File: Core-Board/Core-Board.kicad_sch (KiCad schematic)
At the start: 21 parts, among them J1 POWER, J2 PCIE, J3 XT60-M, J4 PCIE, J5 PCIE, J6 PCIE, J7 Conn_01x19_Male, J8 PCIE, J9 Conn_01x19_Male, SW1 SW_SPST, U1 AP2112K-3.3, U2 74HC4050D, U3 XTSD04GLGEAG, U4 ESP32-DEVKITC-32D

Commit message: more smol updates
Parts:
- removed C4, C5: 10uF, symbol Device:C_Small
- removed R1: 10k, symbol Device:R_Small
- removed U1: AP2112K-3.3, Package_TO_SOT_SMD:SOT-23-5, symbol Regulator_Linear:AP2112K-3.3
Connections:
- net SD VIN is gone; now on net +3.3V: U2.1 (VCC)
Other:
- moved on the sheet: C1, C2, C3, J1, J3

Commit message: core board pinouts
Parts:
- removed C1, C2, C3: 0.1uF, symbol Device:C_Small
- removed J6: PCIE, symbol PCIE:PCIE-LP-01-01-F-DV-A-TR_(card_edge)
- added C10, C4, C9: 22uF, symbol Device:C_Small
- added C5, C6: 2.2uF, symbol Device:C_Small
- added C7, C8: 0.1uF, symbol Device:C_Small
- added D1, D2, D3, D4, D5: D_Small, symbol Device:D_Small
- added F1, F4: 6A Fuse, symbol Device:Polyfuse_Small
- added F2, F3: 500mA Fuse, symbol Device:Polyfuse_Small
- added J10: PCIE, symbol PCIE:PCIE-LP-01-01-F-DV-A-TR_(card_edge)
- added L1: 12uH, symbol Device:L_Small
- added L2: 18, symbol Device:L_Small
- added R1: 10k, symbol Device:R_Small
- added R3: 51k, symbol Device:R_Small
- added R4, R6: 22.1k, symbol Device:R_Small
- added R5: 88.7k, symbol Device:R_Small
- added R7, R8: 1k, symbol Device:R_Small
- added U1, U4: TPS560430X3FDBVT, Package_TO_SOT_SMD:SOT-23-6, symbol Regulator_Switching:TPS560430X3FDBVT
- R2: value R_Small -> 1k
- renumbered U4 to J6
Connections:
- net +12V: now also F1.1; no longer J2.A16, J2.A17, J2.A18, J2.B16, J2.B17, J2.B18, J4.A16, J4.A17, J4.A18, J4.B16, J4.B17, J4.B18, J5.A16, J5.A17, J5.A18, J5.B16, J5.B17, J5.B18, J8.A16, J8.A17, J8.A18, J8.B16, J8.B17, J8.B18
- net +3.3V: no longer J2.B13, J2.B14, J4.B13, J4.B14, J5.B13, J5.B14, J6.1 (3V3), J8.B13, J8.B14
- net +5V: no longer J2.A13, J2.A14, J4.A13, J4.A14, J5.A13, J5.A14, J6.19 (EXT_5V), J8.A13, J8.A14
- net GND: now also J2.A6, J4.A6, J5.A6, J8.A6, C10.1, C4.1, C5.1, C6.1, C9.1, D1.2 (A), D4.2 (A), D5.2 (A), J10.A12, J10.A15, J10.A3, J10.A6, J10.B12, J10.B15, J10.B3, R4.2, R6.2, U1.2 (GND), U4.2 (GND); no longer J2.A7, J2.B4, J2.B8, J4.A7, J4.B4, J4.B8, J5.A7, J5.B4, J5.B8, J8.A7, J8.B4, J8.B8
- net HX CLK: now also J10.A10
- net HX1: now also J2.B4, J4.B4, J5.B4, J8.B4, J10.B4; no longer J2.A4, J4.A4, J5.A4, J8.A4
- net HX2: now also J2.B5, J4.B5, J5.B5, J8.B5, J10.B5; no longer J2.A5, J4.A5, J5.A5, J8.A5
- net HX3: now also J2.B6, J4.B6, J5.B6, J8.B6, J10.B6; no longer J2.A6, J4.A6, J5.A6, J8.A6
- net HX4: now also J2.B7, J4.B7, J5.B7, J8.B7, J10.B7; no longer J2.B5, J4.B5, J5.B5, J8.B5
- net HX5: now also J2.B8, J4.B8, J5.B8, J8.B8, J10.B8; no longer J2.B6, J4.B6, J5.B6, J8.B6
- net HX6: now also J2.A7, J4.A7, J5.A7, J8.A7, J10.A7; no longer J2.B7, J4.B7, J5.B7, J8.B7
- net HX7: now also J10.A8
- net HX8: now also J10.A9
- net MOS SCL: now also J10.A2
- net MOS SDA: now also J10.A1
- net SD CLK: no longer J6.28 (IO18), J9.9 (Pin_9)
- net SD MISO: no longer J6.21 (IO23), J9.2 (Pin_2)
- net TC CLK: now also J2.A4, J4.A4, J5.A4, J8.A4, J10.A4; no longer J2.B1, J4.B1, J5.B1, J8.B1
- net TC MOSI: no longer J2.B2, J4.B2, J5.B2, J6.15 (IO13), J8.B2
- net TC1: now also J10.B9
- net TC2: now also J10.B10
- net TC3: now also J10.B11
- net TC4: now also J10.A11
- new net: C7.2, U1.1 (CB)
- new net: C7.1, D3.1 (K), L2.1, U1.6 (SW)
- new net: C4.2, F1.2, F4.1, R1.1
- new net: C9.2, D2.2 (A), F2.1, L1.2, R3.1
- new net: D5.1 (K), R8.2
- new net: C8.1, D2.1 (K), L1.1, U4.6 (SW)
- new net: C8.2, U4.1 (CB)
- new net: C10.2, D3.2 (A), F3.1, L2.2, R5.1
- new net: D1.1 (K), R1.2
- new net: D4.1 (K), R7.2
- new net 12V: C5.2, C6.2, F4.2, J10.A16, J10.A17, J10.A18, J10.B16, J10.B17, J10.B18, J2.A16, J2.A17, J2.A18, J2.B16, J2.B17, J2.B18, J4.A16, J4.A17, J4.A18, J4.B16, J4.B17, J4.B18, J5.A16, J5.A17, J5.A18, J5.B16, J5.B17, J5.B18, J8.A16, J8.A17, J8.A18, J8.B16, J8.B17, J8.B18, U1.4 (EN), U1.5 (VIN), U4.4 (EN), U4.5 (VIN)
- new net 3.3FB: R3.2, R4.1, U4.3 (FB)
- new net 3.3V: F2.2, J10.B13, J10.B14, J2.B13, J2.B14, J4.B13, J4.B14, J5.B13, J5.B14, J6.1 (3V3), J8.B13, J8.B14, R8.1
- new net 5FB: R5.2, R6.1, U1.3 (FB)
- new net 5V: F3.2, J10.A13, J10.A14, J2.A13, J2.A14, J4.A13, J4.A14, J5.A13, J5.A14, J6.19 (EXT_5V), J8.A13, J8.A14, R7.1
- new net SD, TC CLK: J10.B1, J2.B1, J4.B1, J5.B1, J6.28 (IO18), J8.B1, J9.9 (Pin_9)
- new net SD, TC MISO: J10.B2, J2.B2, J4.B2, J5.B2, J6.21 (IO23), J8.B2, J9.2 (Pin_2)
- new net TC MISO: J10.A5, J2.A5, J4.A5, J5.A5, J6.15 (IO13), J8.A5
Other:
- note added: "Connect to Battery/ Power Supply"
- note added: "Voltage Regulators Overcurrent/ Overvoltage Protection"
- note removed: "Power"
- moved on the sheet: J1, J2, J3, J6, J7, J9, R2, SW1, U2, U3

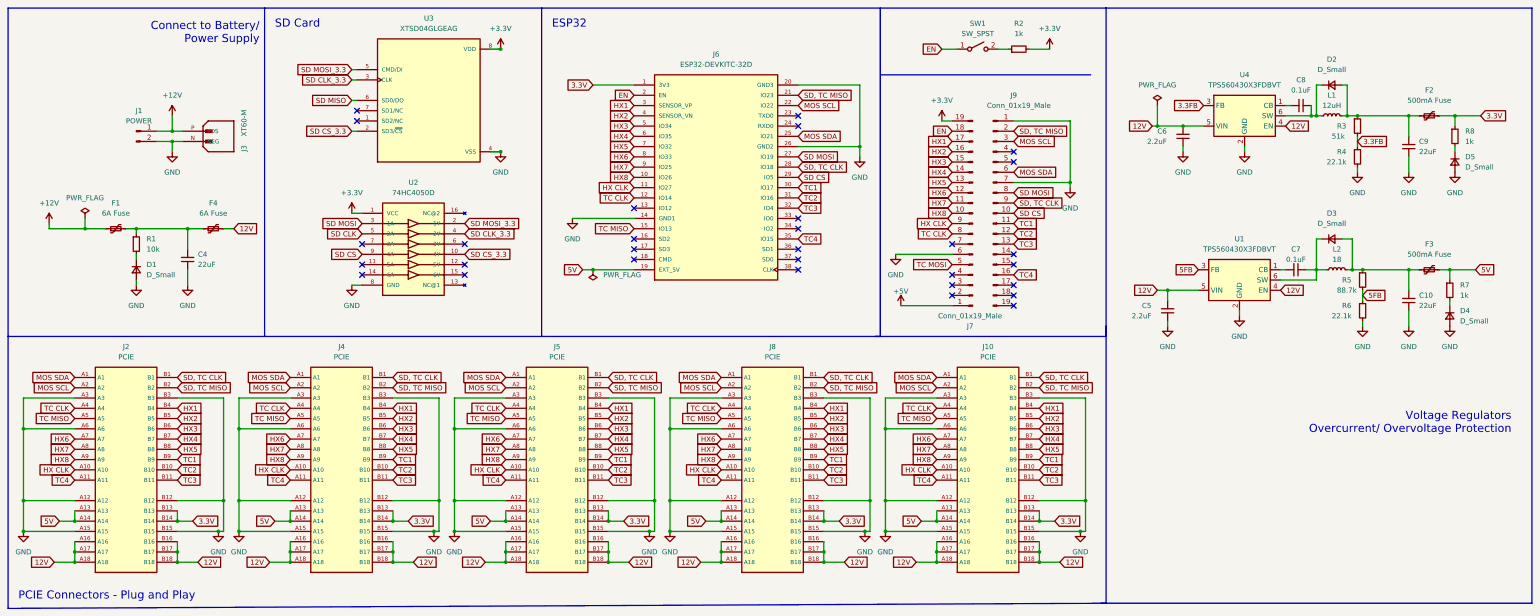
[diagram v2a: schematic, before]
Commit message: Finalize core board schematics.
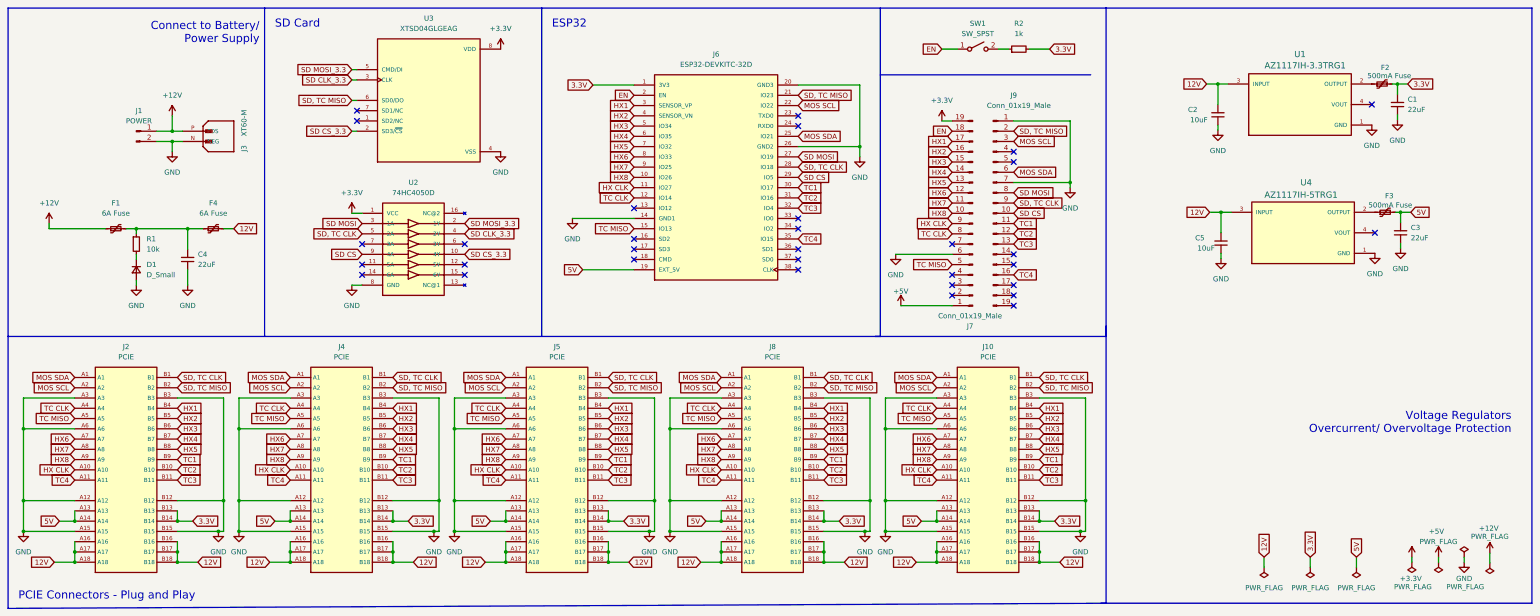
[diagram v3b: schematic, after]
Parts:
- removed C10, C9: 22uF, symbol Device:C_Small
- removed C6: 2.2uF, symbol Device:C_Small
- removed C7, C8: 0.1uF, symbol Device:C_Small
- removed D2, D3, D4, D5: D_Small, symbol Device:D_Small
- removed L1: 12uH, symbol Device:L_Small
- removed L2: 18, symbol Device:L_Small
- removed R3: 51k, symbol Device:R_Small
- removed R4, R6: 22.1k, symbol Device:R_Small
- removed R5: 88.7k, symbol Device:R_Small
- removed R7, R8: 1k, symbol Device:R_Small
- removed U1, U4: TPS560430X3FDBVT, Package_TO_SOT_SMD:SOT-23-6, symbol Regulator_Switching:TPS560430X3FDBVT
- added C1, C3: 22uF, Capacitor_SMD:C_0603_1608Metric, symbol Device:C_Small
- added C2: 10uF, Capacitor_SMD:C_0603_1608Metric, symbol Device:C_Small
- added U1: AZ1117IH-3.3TRG1, AZ1117IH-3:SOT230P700X185-4N, symbol AZ1117IH-3.3TRG1:AZ1117IH-3.3TRG1
- added U4: AZ1117IH-5TRG1, AZ1117IH-3:SOT230P700X185-4N, symbol AZ1117IH-3.3TRG1:AZ1117IH-3.3TRG1
- C4: footprint (none) -> Capacitor_SMD:C_0603_1608Metric
- C5: value 2.2uF -> 10uF; footprint (none) -> Capacitor_SMD:C_0603_1608Metric
- D1: footprint (none) -> Diode_SMD:D_0603_1608Metric
- F1, F4: footprint (none) -> Fuse:Fuse_2920_7451Metric
- F2, F3: footprint (none) -> Fuse:Fuse_0603_1608Metric
- J1: footprint (none) -> Connector:Banana_Jack_2Pin
- J10, J2, J4, J5, J8: footprint (none) -> PCIE_throughhole:AMPHENOL_10018783-11200TLF; MANUFACTURER (none) -> Samtec; MAXIMUM_PACKAGE_HEIGHT (none) -> 8.13mm; PARTREV (none) -> B; STANDARD (none) -> Manufacturer Recommendations
- J3: footprint AMASS_XT60-M -> XT60-M:AMASS_XT60-M
- J6: footprint MODULE_ESP32-DEVKITC-32D -> Ellie_Project_Footprints:MODULE_ESP32-DEVKITC-32D
- J7, J9: footprint (none) -> Connector_PinHeader_1.27mm:PinHeader_1x19_P1.27mm_Vertical
- R1, R2: footprint (none) -> Resistor_SMD:R_0603_1608Metric
- SW1: footprint (none) -> Button_Switch_THT:SW_PUSH_6mm
- U2: footprint SO16 -> 74HC4050D:SO16; Check_prices https://www.snapeda.com/parts/74HC4050D/Toshiba+Semiconduct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 -> https://www.snapeda.com/parts/74HC4050D/Nexperia/view-part/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; MF Toshiba -> Nexperia; Package SOIC-16 Toshiba -> None; SnapEDA_Link https://www.snapeda.com/parts/74HC4050D/Toshiba+Semiconduct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 -> https://www.snapeda.com/parts/74HC4050D/Nexperia/view-part/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
- U3: footprint SON127P600X800X95-8N -> XTSD04GLGEAG:SON127P600X800X95-8N
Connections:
- net SD CLK is gone; now on net SD, TC CLK: U2.5 (2A)
- net SD MISO is gone; now on net SD, TC MISO: U3.6 (SD0/DO)
- net TC MOSI is gone; now on net TC MISO: J7.5 (Pin_5)
- net +3.3V: no longer R2.2
- net 12V: now also C2.2, U1.3 (INPUT), U4.3 (INPUT)
- net 3.3V: now also R2.2, C1.2
- net 5V: now also C3.2
- net GND: now also C1.1, C2.1, C3.1, U1.1 (GND), U4.1 (GND)
- net at F2.1: now also U1.2 (OUTPUT)
- net at F3.1: now also U4.2 (OUTPUT)
- no-connect marks 30 -> 32

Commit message: wired pcie together in core board.
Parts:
- J10, J2, J4, J5, J8: footprint PCIE_throughhole:AMPHENOL_10018783-11200TLF -> 10018784-10210TLF:AMPHENOL_10018784-10210TLF
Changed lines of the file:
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@@
     (property "Reference" "J5" (id 0) (at 158.75 147.32 0))
     (property "Value" "PCIE" (id 1) (at 158.75 149.86 0))
-    (property "Footprint" "PCIE_throughhole:AMPHENOL_10018783-11200TLF" (id 2) (at 157.48 207.01 0)
+    (property "Footprint" "10018784-10210TLF:AMPHENOL_10018784-10210TLF" (id 2) (at 157.48 207.01 0)
       (effects (font (size 1.27 1.27)) hide)
     )
@@
     (property "Reference" "J10" (id 0) (at 265.43 147.32 0))
     (property "Value" "PCIE" (id 1) (at 265.43 149.86 0))
-    (property "Footprint" "PCIE_throughhole:AMPHENOL_10018783-11200TLF" (id 2) (at 264.16 207.01 0)
+    (property "Footprint" "10018784-10210TLF:AMPHENOL_10018784-10210TLF" (id 2) (at 264.16 207.01 0)
       (effects (font (size 1.27 1.27)) hide)
     )
@@
     (property "Reference" "J2" (id 0) (at 52.07 147.32 0))
     (property "Value" "PCIE" (id 1) (at 52.07 149.86 0))
-    (property "Footprint" "PCIE_throughhole:AMPHENOL_10018783-11200TLF" (id 2) (at 50.8 207.01 0)
+    (property "Footprint" "10018784-10210TLF:AMPHENOL_10018784-10210TLF" (id 2) (at 50.8 207.01 0)
       (effects (font (size 1.27 1.27)) hide)
     )
@@
     (property "Reference" "J8" (id 0) (at 212.09 147.32 0))
     (property "Value" "PCIE" (id 1) (at 212.09 149.86 0))
-    (property "Footprint" "PCIE_throughhole:AMPHENOL_10018783-11200TLF" (id 2) (at 210.82 207.01 0)
+    (property "Footprint" "10018784-10210TLF:AMPHENOL_10018784-10210TLF" (id 2) (at 210.82 207.01 0)
       (effects (font (size 1.27 1.27)) hide)
     )
@@
     (property "Reference" "J4" (id 0) (at 105.41 147.32 0))
     (property "Value" "PCIE" (id 1) (at 105.41 149.86 0))
-    (property "Footprint" "PCIE_throughhole:AMPHENOL_10018783-11200TLF" (id 2) (at 104.14 207.01 0)
+    (property "Footprint" "10018784-10210TLF:AMPHENOL_10018784-10210TLF" (id 2) (at 104.14 207.01 0)
       (effects (font (size 1.27 1.27)) hide)
     )
@@
     )
     (path "/96b9cdb6-15db-4919-bc6e-d568351af155"
-      (reference "J2") (unit 1) (value "PCIE") (footprint "PCIE_throughhole:AMPHENOL_10018783-11200TLF")
+      (reference "J2") (unit 1) (value "PCIE") (footprint "10018784-10210TLF:AMPHENOL_10018784-10210TLF")
     )
     (path "/cb45fbf9-ba1c-4c10-92c7-cc39f699f73a"
@@
     )
     (path "/e918744b-b12c-4b95-a404-7b5236770a01"
-      (reference "J4") (unit 1) (value "PCIE") (footprint "PCIE_throughhole:AMPHENOL_10018783-11200TLF")
+      (reference "J4") (unit 1) (value "PCIE") (footprint "10018784-10210TLF:AMPHENOL_10018784-10210TLF")
     )
     (path "/1c43319e-7373-4e42-8c0b-9621338797a5"
-      (reference "J5") (unit 1) (value "PCIE") (footprint "PCIE_throughhole:AMPHENOL_10018783-11200TLF")
+      (reference "J5") (unit 1) (value "PCIE") (footprint "10018784-10210TLF:AMPHENOL_10018784-10210TLF")
     )
     (path "/9915a168-b5b5-4cc9-a845-d62f1365f20e"
@@
     )
     (path "/d3636d21-c771-40d8-9746-b5c1c32e4f3d"
-      (reference "J8") (unit 1) (value "PCIE") (footprint "PCIE_throughhole:AMPHENOL_10018783-11200TLF")
+      (reference "J8") (unit 1) (value "PCIE") (footprint "10018784-10210TLF:AMPHENOL_10018784-10210TLF")
     )
     (path "/178070bc-9e77-447a-b349-b952957ba5f5"
@@
     )
     (path "/54c4d0ab-46f9-43c0-898c-6a220b8fa724"
-      (reference "J10") (unit 1) (value "PCIE") (footprint "PCIE_throughhole:AMPHENOL_10018783-11200TLF")
+      (reference "J10") (unit 1) (value "PCIE") (footprint "10018784-10210TLF:AMPHENOL_10018784-10210TLF")
     )
     (path "/fcbb5a27-40ec-4170-896c-a481825968e6"
